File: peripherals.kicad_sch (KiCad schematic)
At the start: 28 parts, among them J7 Conn_01x04, J8 Conn_01x06, J9 Conn_01x06, U10 MPU-6050, U11 TB6612FNG

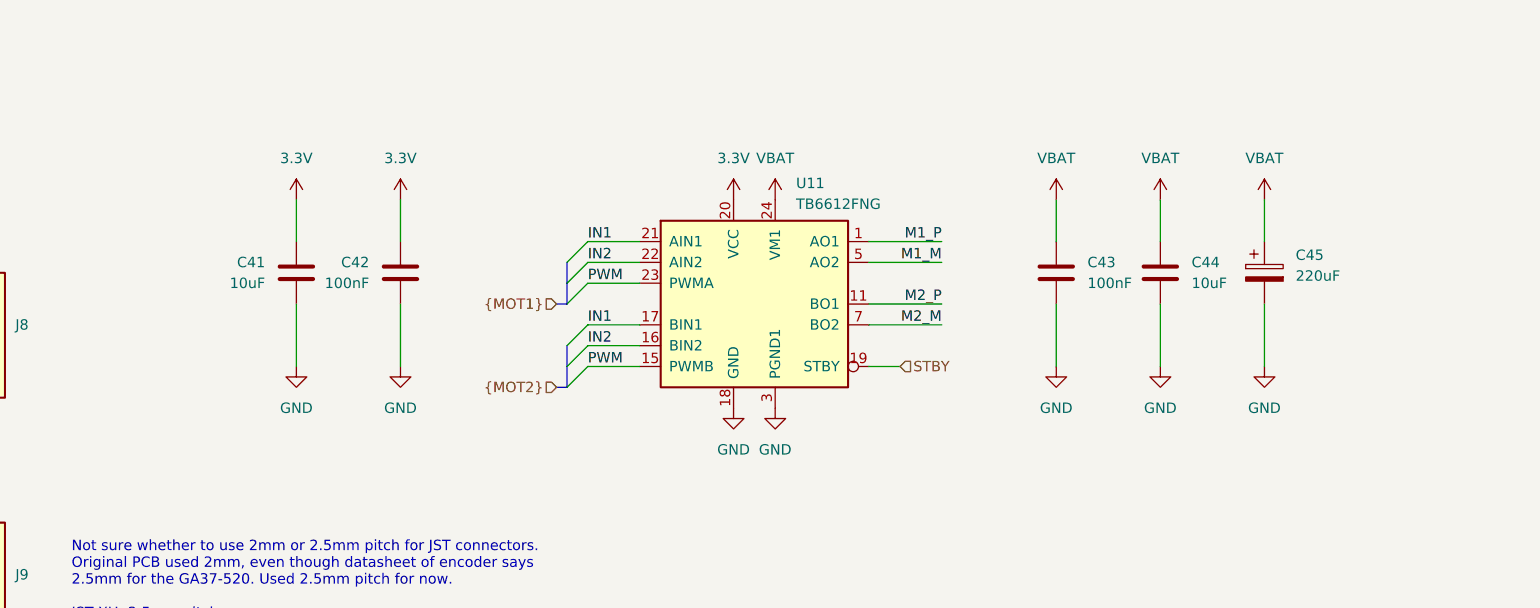
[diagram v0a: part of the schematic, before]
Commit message: Add additional bulk cap for motors
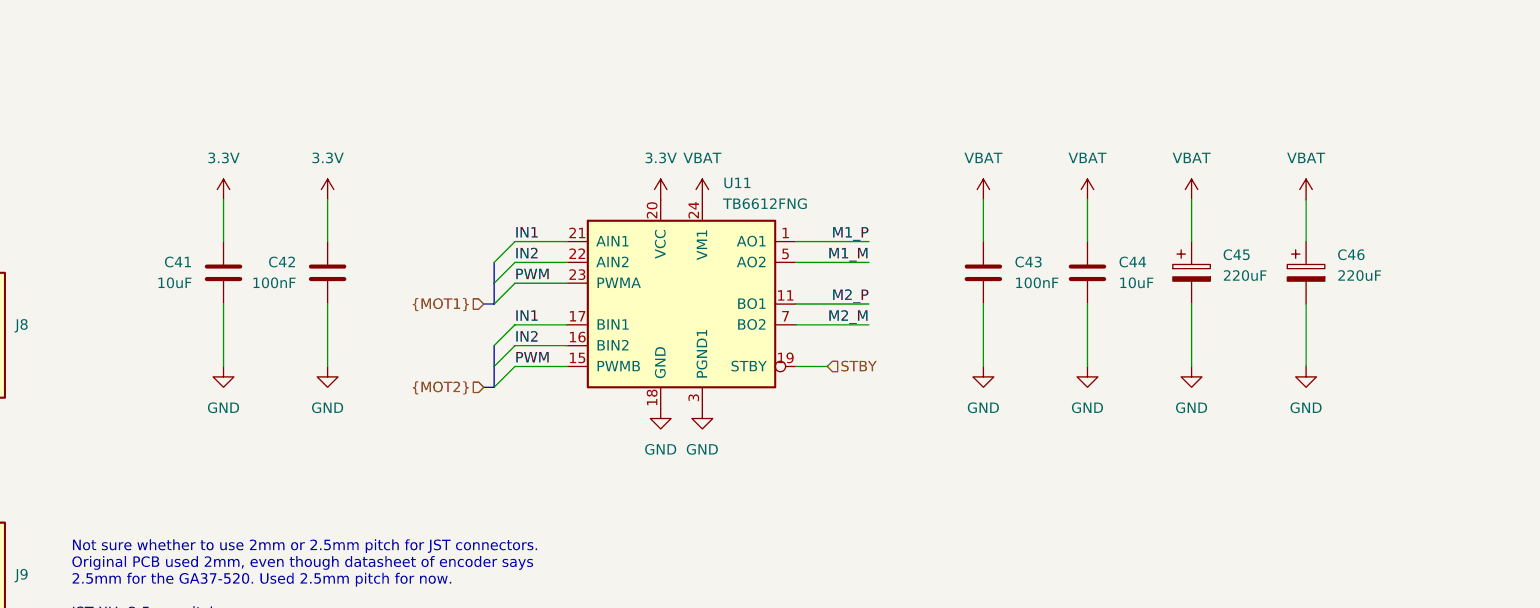
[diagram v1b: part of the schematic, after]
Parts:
- added C46: 220uF, Capacitor_SMD:CP_Elec_10x10, symbol Device:C_Polarized
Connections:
- net GND: now also C46.2
- net VBAT: now also C46.1
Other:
- moved on the sheet: C41, C42, C43, C44, C45, U11

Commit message: Set footprint for test points
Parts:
- TP11, TP12: footprint (none) -> TestPoint:TestPoint_Pad_D1.5mm
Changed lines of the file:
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@@
 			)
 		)
-		(property "Footprint" ""
+		(property "Footprint" "TestPoint:TestPoint_Pad_D1.5mm"
 			(at 219.71 48.26 0)
 			(effects
@@
 			)
 		)
-		(property "Footprint" ""
+		(property "Footprint" "TestPoint:TestPoint_Pad_D1.5mm"
 			(at 199.39 48.26 0)
 			(effects

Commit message: Fix net connection bug
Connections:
- net ENCA: no longer R26.2, R30.2
- net at J8.3 (Pin_3), R23.1: now also R26.2
- net at J9.3 (Pin_3), R27.1: now also R30.2
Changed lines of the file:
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@@
-	)
-	(junction
-		(at 67.31 124.46)
-		(diameter 0)
-		(color 0 0 0 0)
 	)
 	(junction
@@
 	)
 	(junction
+		(at 67.31 121.92)
+		(diameter 0)
+		(color 0 0 0 0)
+	)
+	(junction
 		(at 106.68 58.42)
 		(diameter 0)
@@
 	)
 	(junction
-		(at 67.31 154.94)
+		(at 67.31 152.4)
 		(diameter 0)
 		(color 0 0 0 0)
@@
 	(wire
 		(pts
+			(xy 67.31 152.4) (xy 67.31 156.21)
+		)
+		(stroke
+			(width 0)
+			(type default)
+		)
+	)
+	(wire
+		(pts
 			(xy 157.48 121.92) (xy 163.83 121.92)
 		)
@@
 	(wire
 		(pts
-			(xy 64.77 121.92) (xy 88.9 121.92)
+			(xy 64.77 121.92) (xy 67.31 121.92)
 		)
 		(stroke
@@
 	(wire
 		(pts
+			(xy 67.31 121.92) (xy 88.9 121.92)
+		)
+		(stroke
+			(width 0)
+			(type default)
+		)
+	)
+	(wire
+		(pts
 			(xy 106.68 50.8) (xy 107.95 50.8)
 		)
@@
 	(wire
 		(pts
-			(xy 67.31 154.94) (xy 69.85 154.94)
-		)
-		(stroke
-			(width 0)
-			(type default)
-		)
-	)
-	(wire
-		(pts
-			(xy 67.31 124.46) (xy 67.31 125.73)
-		)
-		(stroke
-			(width 0)
-			(type default)
-		)
-	)
-	(wire
-		(pts
 			(xy 227.33 106.68) (xy 227.33 111.76)
 		)
@@
 	(wire
 		(pts
+			(xy 67.31 121.92) (xy 67.31 125.73)
+		)
+		(stroke
+			(width 0)
+			(type default)
+		)
+	)
+	(wire
+		(pts
 			(xy 45.72 152.4) (xy 57.15 152.4)
 		)
@@
 	(wire
 		(pts
-			(xy 54.61 154.94) (xy 67.31 154.94)
+			(xy 54.61 154.94) (xy 69.85 154.94)
 		)
 		(stroke
@@
 	(wire
 		(pts
+			(xy 67.31 152.4) (xy 88.9 152.4)
+		)
+		(stroke
+			(width 0)
+			(type default)
+		)
+	)
+	(wire
+		(pts
 			(xy 158.75 45.72) (xy 156.21 45.72)
 		)
@@
 	(wire
 		(pts
-			(xy 67.31 124.46) (xy 69.85 124.46)
-		)
-		(stroke
-			(width 0)
-			(type default)
-		)
-	)
-	(wire
-		(pts
 			(xy 83.82 45.72) (xy 83.82 49.53)
 		)
@@
 	(wire
 		(pts
-			(xy 67.31 154.94) (xy 67.31 156.21)
-		)
-		(stroke
-			(width 0)
-			(type default)
-		)
-	)
-	(wire
-		(pts
 			(xy 214.63 127) (xy 214.63 119.38)
 		)
@@
 	(wire
 		(pts
-			(xy 54.61 124.46) (xy 67.31 124.46)
+			(xy 54.61 124.46) (xy 69.85 124.46)
 		)
 		(stroke
@@
 	(wire
 		(pts
-			(xy 64.77 152.4) (xy 88.9 152.4)
-		)
-		(stroke
+			(xy 64.77 152.4) (xy 67.31 152.4)
+		)
+		(stroke

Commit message: Fix net connection bug
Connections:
- net ENCA: now also R26.2, R30.2; no longer R25.2, R29.2
- net ENCB: now also R25.2, R29.2
- net at J9.3 (Pin_3), R27.1: no longer R30.2
- net at J8.3 (Pin_3), R23.1: no longer R26.2
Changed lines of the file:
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@@
+	)
+	(junction
+		(at 54.61 152.4)
+		(diameter 0)
+		(color 0 0 0 0)
 	)
 	(junction
@@
 	)
 	(junction
-		(at 67.31 121.92)
-		(diameter 0)
-		(color 0 0 0 0)
-	)
-	(junction
 		(at 106.68 58.42)
 		(diameter 0)
@@
 	)
 	(junction
-		(at 54.61 124.46)
+		(at 67.31 154.94)
 		(diameter 0)
 		(color 0 0 0 0)
 	)
 	(junction
-		(at 67.31 152.4)
+		(at 54.61 121.92)
 		(diameter 0)
 		(color 0 0 0 0)
@@
 	)
 	(junction
-		(at 54.61 154.94)
+		(at 67.31 124.46)
 		(diameter 0)
 		(color 0 0 0 0)
@@
 	(wire
 		(pts
+			(xy 67.31 154.94) (xy 67.31 156.21)
+		)
+		(stroke
+			(width 0)
+			(type default)
+		)
+	)
+	(wire
+		(pts
 			(xy 147.32 45.72) (xy 156.21 45.72)
 		)
@@
 		)
 	)
+	(wire
+		(pts
+			(xy 67.31 124.46) (xy 67.31 125.73)
+		)
+		(stroke
+			(width 0)
+			(type default)
+		)
+	)
 	(bus
 		(pts
@@
 	(wire
 		(pts
-			(xy 67.31 152.4) (xy 67.31 156.21)
-		)
-		(stroke
-			(width 0)
-			(type default)
-		)
-	)
-	(wire
-		(pts
 			(xy 157.48 121.92) (xy 163.83 121.92)
 		)
@@
 	(wire
 		(pts
-			(xy 45.72 121.92) (xy 57.15 121.92)
-		)
-		(stroke
-			(width 0)
-			(type default)
-		)
-	)
-	(wire
-		(pts
-			(xy 64.77 121.92) (xy 67.31 121.92)
+			(xy 45.72 121.92) (xy 54.61 121.92)
 		)
 		(stroke
@@
 	(wire
 		(pts
+			(xy 67.31 124.46) (xy 69.85 124.46)
+		)
+		(stroke
+			(width 0)
+			(type default)
+		)
+	)
+	(wire
+		(pts
 			(xy 204.47 53.34) (xy 204.47 52.07)
 		)
@@
 	(wire
 		(pts
-			(xy 67.31 121.92) (xy 88.9 121.92)
+			(xy 64.77 121.92) (xy 88.9 121.92)
 		)
 		(stroke
@@
 		)
 	)
+	(wire
+		(pts
+			(xy 67.31 154.94) (xy 69.85 154.94)
+		)
+		(stroke
+			(width 0)
+			(type default)
+		)
+	)
 	(bus
 		(pts
@@
 	(wire
 		(pts
-			(xy 67.31 121.92) (xy 67.31 125.73)
-		)
-		(stroke
-			(width 0)
-			(type default)
-		)
-	)
-	(wire
-		(pts
-			(xy 45.72 152.4) (xy 57.15 152.4)
+			(xy 45.72 152.4) (xy 54.61 152.4)
 		)
 		(stroke
@@
 	(wire
 		(pts
+			(xy 54.61 152.4) (xy 54.61 156.21)
+		)
+		(stroke
+			(width 0)
+			(type default)
+		)
+	)
+	(wire
+		(pts
 			(xy 147.32 71.12) (xy 147.32 69.85)
 		)
@@
 	(wire
 		(pts
-			(xy 54.61 154.94) (xy 69.85 154.94)
+			(xy 45.72 154.94) (xy 67.31 154.94)
 		)
 		(stroke
@@
 	(wire
 		(pts
-			(xy 54.61 124.46) (xy 54.61 125.73)
-		)
-		(stroke
-			(width 0)
-			(type default)
-		)
-	)
-	(wire
-		(pts
-			(xy 45.72 124.46) (xy 54.61 124.46)
-		)
-		(stroke
-			(width 0)
-			(type default)
-		)
-	)
-	(wire
-		(pts
-			(xy 67.31 152.4) (xy 88.9 152.4)
+			(xy 45.72 124.46) (xy 67.31 124.46)
+		)
+		(stroke
+			(width 0)
+			(type default)
+		)
+	)
+	(wire
+		(pts
+			(xy 64.77 152.4) (xy 88.9 152.4)
 		)
 		(stroke
@@
 	(wire
 		(pts
+			(xy 54.61 152.4) (xy 57.15 152.4)
+		)
+		(stroke
+			(width 0)
+			(type default)
+		)
+	)
+	(wire
+		(pts
 			(xy 204.47 48.26) (xy 204.47 52.07)
 		)
@@
 	(wire
 		(pts
-			(xy 45.72 154.94) (xy 54.61 154.94)
-		)
-		(stroke
-			(width 0)
-			(type default)
-		)
-	)
-	(wire
-		(pts
 			(xy 157.48 116.84) (xy 163.83 116.84)
 		)
@@
 	(wire
 		(pts
+			(xy 54.61 121.92) (xy 54.61 125.73)
+		)
+		(stroke
+			(width 0)
+			(type default)
+		)
+	)
+	(wire
+		(pts
 			(xy 160.02 69.85) (xy 160.02 71.12)
 		)
@@
 	(wire
 		(pts
-			(xy 54.61 124.46) (xy 69.85 124.46)
-		)
-		(stroke
-			(width 0)
-			(type default)
-		)
-	)
-	(wire
-		(pts
 			(xy 224.79 49.53) (xy 229.87 49.53)
 		)
@@
 		)
 	)
+	(wire
+		(pts
+			(xy 54.61 121.92) (xy 57.15 121.92)
+		)
+		(stroke
+			(width 0)
+			(type default)
+		)
+	)
 	(bus
 		(pts
@@
 	(wire
 		(pts
-			(xy 54.61 154.94) (xy 54.61 156.21)
-		)
-		(stroke
-			(width 0)
-			(type default)
-		)
-	)
-	(wire
-		(pts
 			(xy 214.63 52.07) (xy 229.87 52.07)
 		)
@@
 		)
 		(stroke
-			(width 0)
-			(type default)
-		)
-	)
-	(wire
-		(pts
-			(xy 64.77 152.4) (xy 67.31 152.4)
-		)
-		(stroke

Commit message: Make lcsc field compatible with plugin
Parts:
- C37, C39, C42, C43: LCSC PN (none) -> C14663; LCSC Part C14663 -> (none)
- C38: LCSC PN (none) -> C100042; LCSC Part C100042 -> (none)
- C40: LCSC PN (none) -> C107043; LCSC Part C107043 -> (none)
- C41, C44: LCSC PN (none) -> C96446; LCSC Part C96446 -> (none)
- C45, C46: LCSC PN (none) -> C250054; LCSC Part C250054 -> (none)
- J7: LCSC PN (none) -> C5116530; LCSC Part C5116530 -> (none)
- J8, J9: LCSC PN (none) -> C191914; LCSC Part C191914 -> (none)
- R20: LCSC PN (none) -> C98220; LCSC Part C98220 -> (none)
- R21, R23, R24, R27, R28: LCSC PN (none) -> C185354; LCSC Part C185354 -> (none)
- R22, R25, R26, R29, R30: LCSC PN (none) -> C108078; LCSC Part C108078 -> (none)
- U10: LCSC PN (none) -> C24112; LCSC Part C24112 -> (none)
- U11: LCSC PN (none) -> C141517; LCSC Part C141517 -> (none)
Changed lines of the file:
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@@
 			)
 		)
-		(property "LCSC Part" "C5116530"
+		(property "LCSC PN" "C5116530"
 			(at 234.95 49.53 0)
 			(effects
@@
 			)
 		)
-		(property "LCSC Part" "C108078"
+		(property "LCSC PN" "C108078"
 			(at 67.31 160.02 0)
 			(effects
@@
 			)
 		)
-		(property "LCSC Part" "C14663"
+		(property "LCSC PN" "C14663"
 			(at 69.85 41.91 0)
 			(effects
@@
 			)
 		)
-		(property "LCSC Part" "C108078"
+		(property "LCSC PN" "C108078"
 			(at 54.61 129.54 0)
 			(effects
@@
 			)
 		)
-		(property "LCSC Part" "C14663"
+		(property "LCSC PN" "C14663"
 			(at 134.62 115.57 0)
 			(effects
@@
 			)
 		)
-		(property "LCSC Part" "C98220"
+		(property "LCSC PN" "C98220"
 			(at 147.32 40.64 0)
 			(effects
@@
 			)
 		)
-		(property "LCSC Part" "C185354"
+		(property "LCSC PN" "C185354"
 			(at 60.96 121.92 90)
 			(effects
@@
 			)
 		)
-		(property "LCSC Part" "C191914"
+		(property "LCSC PN" "C191914"
 			(at 93.98 152.4 0)
 			(effects
@@
 			)
 		)
-		(property "LCSC Part" "C250054"
+		(property "LCSC PN" "C250054"
 			(at 254 115.57 0)
 			(effects
@@
 			)
 		)
-		(property "LCSC Part" "C141517"
+		(property "LCSC PN" "C141517"
 			(at 177.8 119.38 0)
 			(effects
@@
 			)
 		)
-		(property "LCSC Part" "C96446"
+		(property "LCSC PN" "C96446"
 			(at 227.33 115.57 0)
 			(effects
@@
 			)
 		)
-		(property "LCSC Part" "C185354"
+		(property "LCSC PN" "C185354"
 			(at 210.82 52.07 90)
 			(effects
@@
 			)
 		)
-		(property "LCSC Part" "C185354"
+		(property "LCSC PN" "C185354"
 			(at 60.96 152.4 90)
 			(effects
@@
 			)
 		)
-		(property "LCSC Part" "C108078"
+		(property "LCSC PN" "C108078"
 			(at 54.61 160.02 0)
 			(effects
@@
 			)
 		)
-		(property "LCSC Part" "C107043"
+		(property "LCSC PN" "C107043"
 			(at 160.02 66.04 0)
 			(effects
@@
 			)
 		)
-		(property "LCSC Part" "C108078"
+		(property "LCSC PN" "C108078"
 			(at 204.47 57.15 0)
 			(effects
@@
 			)
 		)
-		(property "LCSC Part" "C24112"
+		(property "LCSC PN" "C24112"
 			(at 125.73 53.34 0)
 			(effects
@@
 			)
 		)
-		(property "LCSC Part" "C185354"
+		(property "LCSC PN" "C185354"
 			(at 73.66 124.46 90)
 			(effects
@@
 			)
 		)
-		(property "LCSC Part" "C250054"
+		(property "LCSC PN" "C250054"
 			(at 240.03 115.57 0)
 			(effects
@@
 			)
 		)
-		(property "LCSC Part" "C191914"
+		(property "LCSC PN" "C191914"
 			(at 93.98 121.92 0)
 			(effects
@@
 			)
 		)
-		(property "LCSC Part" "C14663"
+		(property "LCSC PN" "C14663"
 			(at 214.63 115.57 0)
 			(effects
@@
 			)
 		)
-		(property "LCSC Part" "C108078"
+		(property "LCSC PN" "C108078"
 			(at 67.31 129.54 0)
 			(effects
@@
 			)
 		)
-		(property "LCSC Part" "C14663"
+		(property "LCSC PN" "C14663"
 			(at 147.32 66.04 0)
 			(effects
@@
 			)
 		)
-		(property "LCSC Part" "C185354"
+		(property "LCSC PN" "C185354"
 			(at 73.66 154.94 90)
 			(effects
@@
 			)
 		)
-		(property "LCSC Part" "C96446"
+		(property "LCSC PN" "C96446"
 			(at 121.92 115.57 0)
 			(effects
@@
 			)
 		)
-		(property "LCSC Part" "C100042"
+		(property "LCSC PN" "C100042"
 			(at 83.82 41.91 0)
 			(effects

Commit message: Exclude test points from BOM
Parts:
- TP10, TP11, TP12: now left out of the parts list
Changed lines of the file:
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@@
 		(unit 1)
 		(exclude_from_sim no)
-		(in_bom yes)
+		(in_bom no)
 		(on_board yes)
 		(dnp no)
@@
 		(unit 1)
 		(exclude_from_sim no)
-		(in_bom yes)
+		(in_bom no)
 		(on_board yes)
 		(dnp no)
@@
 		(unit 1)
 		(exclude_from_sim no)
-		(in_bom yes)
-		(on_board yes)
-		(dnp no)
+		(in_bom no)
+		(on_board yes)
+		(dnp no)

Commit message: Add missing rgb leds
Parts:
- renumbered C37 to C32, C38 to C33, C39 to C34, C40 to C35, C41 to C36, C42 to C37, C43 to C38, C44 to C39, C45 to C40, C46 to C41, R20 to R19, R21 to R20, R22 to R21, R23 to R22, R24 to R23, R25 to R24, R26 to R25, R27 to R26, R28 to R27, R29 to R28, R30 to R29
